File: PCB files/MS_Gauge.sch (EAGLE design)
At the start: 27 parts, among them IC1 B1836M, IC2 LPC11C24_QFP48, U1 MCP1700, U2 TSR1-2450, Y1 12MHz

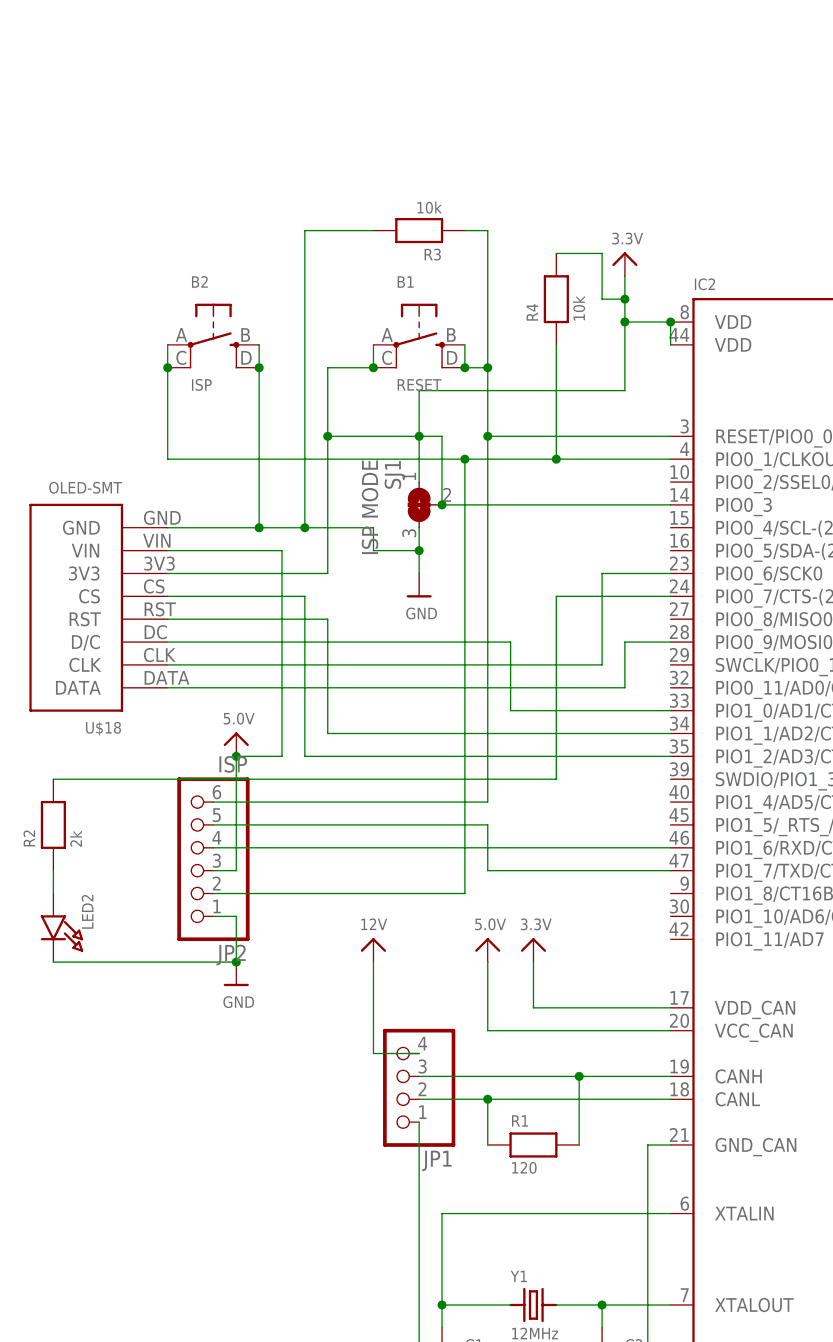
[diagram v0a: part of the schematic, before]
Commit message: Update Eagle files to Rev 4. Fixes wrong reset button wiring, adds termination resistor solder jumper.
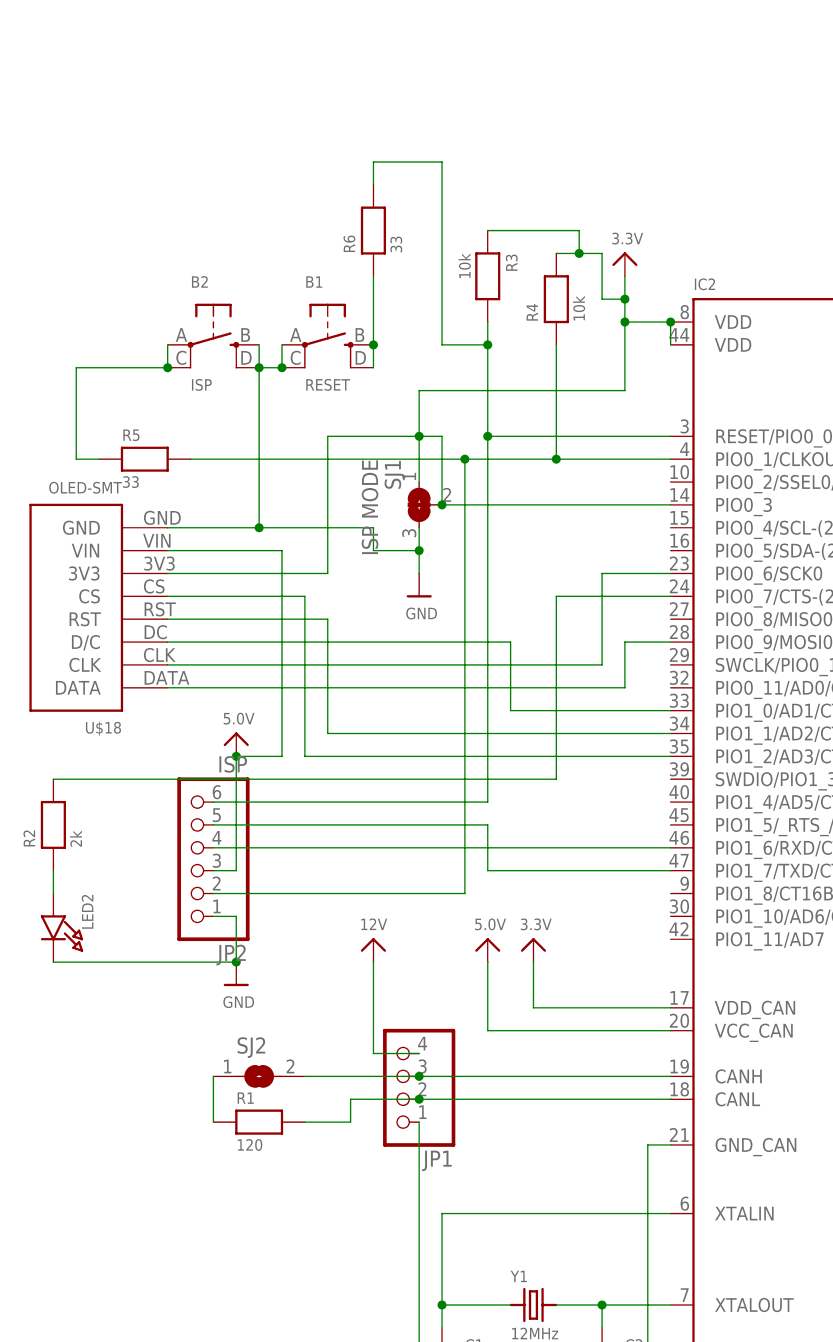
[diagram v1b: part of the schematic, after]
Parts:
- added R5, R6: 33, microbuilder:RESISTOR0603
- added SJ2: (no value), microbuilder:SOLDERJUMPER
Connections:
- new net N$17: IC2.CANH, JP1.3, SJ2.2
- new net N$6: IC2.PIO0_1/CLKOUT/CT32B0_MAT2, JP2.2, R4.1, R5.2
- new net N$8: B1.S, B1.S1, R6.1
- net 3.3V: now also R3.1; no longer B1.P, B1.P1
- net GND: now also B1.P, B1.P1; no longer R3.2
- net N$1: now also R1.1, SJ2.1; no longer IC2.CANH, JP1.3, R1.2
- net N$13: now also R3.2, R6.2; no longer B1.S, B1.S1, R3.1
- net N$2: now also R1.2; no longer R1.1
- net N$5: now also R5.1; no longer IC2.PIO0_1/CLKOUT/CT32B0_MAT2, JP2.2, R4.1
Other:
- moved on the sheet: B1, R1, R3

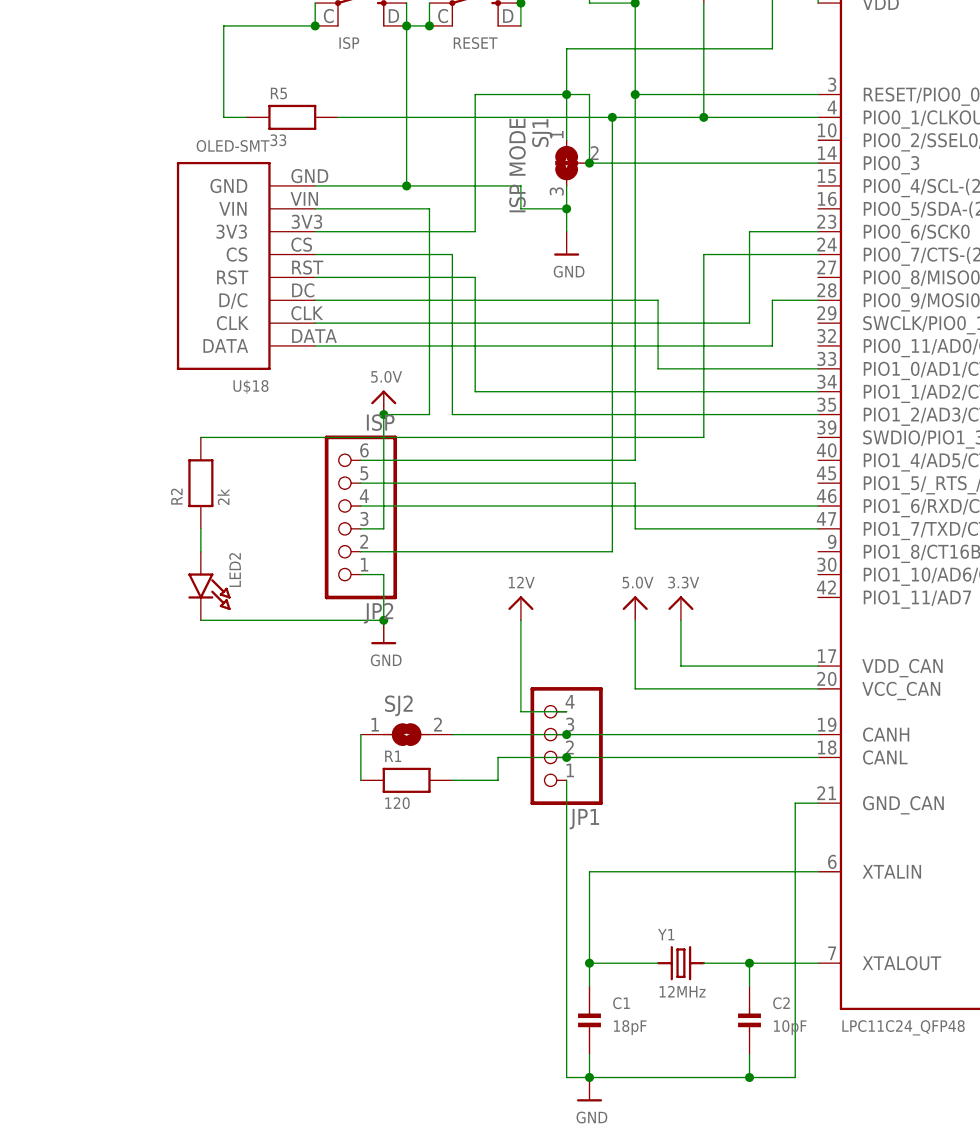
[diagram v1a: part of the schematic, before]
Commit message: Update Eagle files to Rev 5. Adds i2c eeprom.
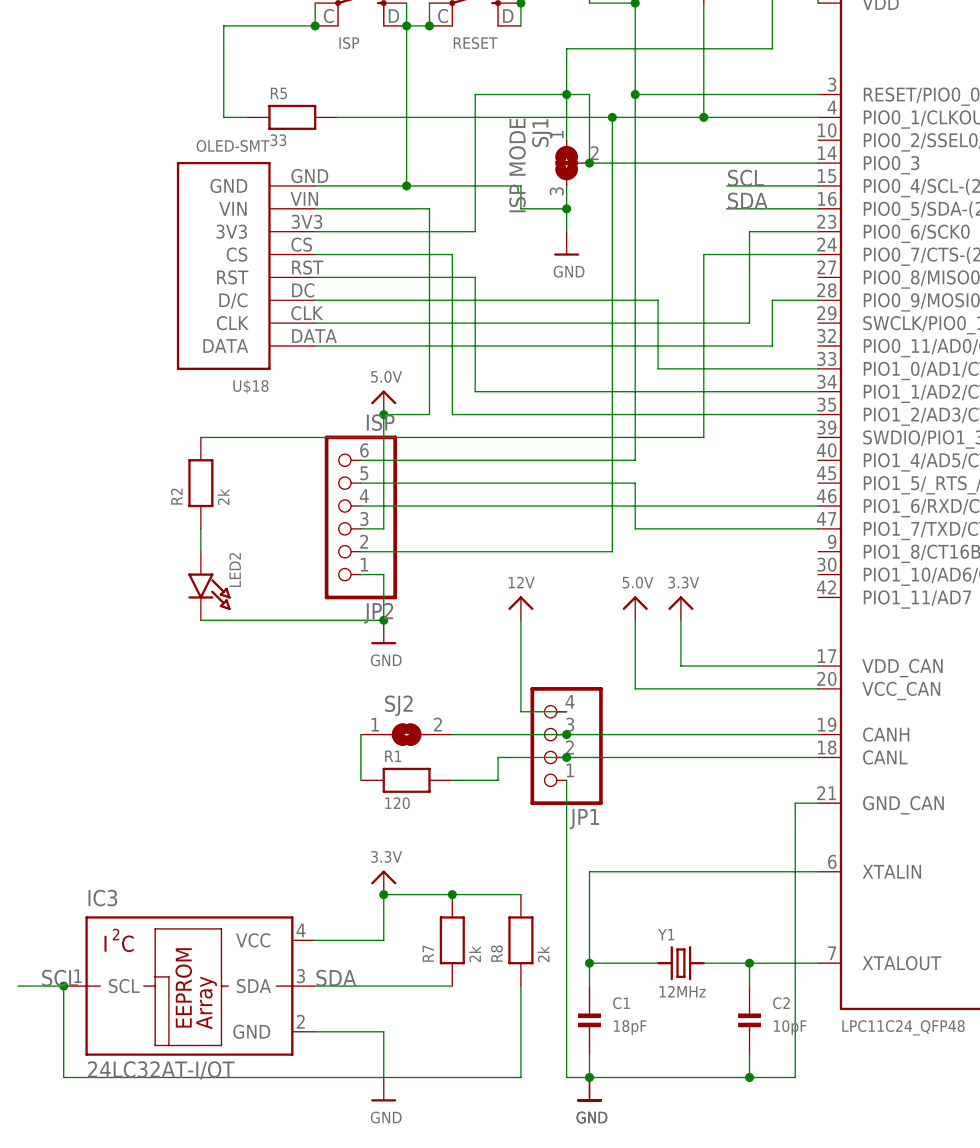
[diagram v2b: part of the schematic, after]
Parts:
- added IC3: 24LC32AT-I/OT, microchip:24LC32AT-I/OT
- added R7, R8: 2k, microbuilder:RESISTOR0603
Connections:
- new net SCL: IC2.PIO0_4/SCL-(20MA_SINK), IC3.SCL, R8.1
- new net SDA: IC2.PIO0_5/SDA-(20MA_SINK), IC3.SDA, R7.1
- net 3.3V: now also IC3.VCC, R7.2, R8.2
- net GND: now also IC3.GND
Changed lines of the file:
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@@
 <grid distance="0.1" unitdist="inch" unit="inch" style="lines" multiple="1" display="no" altdistance="0.01" altunitdist="inch" altunit="inch"/>
 <layers>
-<layer number="1" name="Top" color="4" fill="1" visible="no" active="no"/>
-<layer number="16" name="Bottom" color="1" fill="1" visible="no" active="no"/>
-<layer number="17" name="Pads" color="2" fill="1" visible="no" active="no"/>
-<layer number="18" name="Vias" color="2" fill="1" visible="no" active="no"/>
-<layer number="19" name="Unrouted" color="6" fill="1" visible="no" active="no"/>
-<layer number="20" name="Dimension" color="15" fill="1" visible="no" active="no"/>
-<layer number="21" name="tPlace" color="7" fill="1" visible="no" active="no"/>
-<layer number="22" name="bPlace" color="7" fill="1" visible="no" active="no"/>
-<layer number="23" name="tOrigins" color="15" fill="1" visible="no" active="no"/>
-<layer number="24" name="bOrigins" color="15" fill="1" visible="no" active="no"/>
-<layer number="25" name="tNames" color="7" fill="1" visible="no" active="no"/>
-<layer number="26" name="bNames" color="7" fill="1" visible="no" active="no"/>
-<layer number="27" name="tValues" color="7" fill="1" visible="no" active="no"/>
-<layer number="28" name="bValues" color="7" fill="1" visible="no" active="no"/>
+<layer number="1" name="Top" color="4" fill="1" visible="yes" active="no"/>
+<layer number="16" name="Bottom" color="1" fill="1" visible="yes" active="no"/>
+<layer number="17" name="Pads" color="2" fill="1" visible="yes" active="no"/>
+<layer number="18" name="Vias" color="2" fill="1" visible="yes" active="no"/>
+<layer number="19" name="Unrouted" color="6" fill="1" visible="yes" active="no"/>
+<layer number="20" name="Dimension" color="15" fill="1" visible="yes" active="no"/>
+<layer number="21" name="tPlace" color="7" fill="1" visible="yes" active="no"/>
+<layer number="22" name="bPlace" color="7" fill="1" visible="yes" active="no"/>
+<layer number="23" name="tOrigins" color="15" fill="1" visible="yes" active="no"/>
+<layer number="24" name="bOrigins" color="15" fill="1" visible="yes" active="no"/>
+<layer number="25" name="tNames" color="7" fill="1" visible="yes" active="no"/>
+<layer number="26" name="bNames" color="7" fill="1" visible="yes" active="no"/>
+<layer number="27" name="tValues" color="7" fill="1" visible="yes" active="no"/>
+<layer number="28" name="bValues" color="7" fill="1" visible="yes" active="no"/>
 <layer number="29" name="tStop" color="7" fill="3" visible="no" active="no"/>
 <layer number="30" name="bStop" color="7" fill="6" visible="no" active="no"/>
@@
 <layer number="35" name="tGlue" color="7" fill="4" visible="no" active="no"/>
 <layer number="36" name="bGlue" color="7" fill="5" visible="no" active="no"/>
-<layer number="37" name="tTest" color="7" fill="1" visible="no" active="no"/>
-<layer number="38" name="bTest" color="7" fill="1" visible="no" active="no"/>
+<layer number="37" name="tTest" color="7" fill="1" visible="yes" active="no"/>
+<layer number="38" name="bTest" color="7" fill="1" visible="yes" active="no"/>
 <layer number="39" name="tKeepout" color="4" fill="11" visible="no" active="no"/>
 <layer number="40" name="bKeepout" color="1" fill="11" visible="no" active="no"/>
@@
 <layer number="44" name="Drills" color="7" fill="1" visible="no" active="no"/>
 <layer number="45" name="Holes" color="7" fill="1" visible="no" active="no"/>
-<layer number="46" name="Milling" color="3" fill="1" visible="no" active="no"/>
-<layer number="47" name="Measures" color="7" fill="1" visible="no" active="no"/>
-<layer number="48" name="Document" color="7" fill="1" visible="no" active="no"/>
-<layer number="49" name="Reference" color="7" fill="1" visible="no" active="no"/>
-<layer number="50" name="dxf" color="7" fill="1" visible="no" active="no"/>
-<layer number="51" name="tDocu" color="7" fill="1" visible="no" active="no"/>
-<layer number="52" name="bDocu" color="7" fill="1" visible="no" active="no"/>
-<layer number="53" name="tGND_GNDA" color="7" fill="9" visible="no" active="no"/>
-<layer number="54" name="bGND_GNDA" color="1" fill="9" visible="no" active="no"/>
-<layer number="56" name="wert" color="7" fill="1" visible="no" active="no"/>
-<layer number="57" name="tCAD" color="7" fill="1" visible="no" active="no"/>
-<layer number="59" name="tCarbon" color="7" fill="1" visible="no" active="no"/>
-<layer number="60" name="bCarbon" color="7" fill="1" visible="no" active="no"/>
+<layer number="46" name="Milling" color="3" fill="1" visible="yes" active="no"/>
+<layer number="47" name="Measures" color="7" fill="1" visible="yes" active="no"/>
+<layer number="48" name="Document" color="7" fill="1" visible="yes" active="no"/>
+<layer number="49" name="Reference" color="7" fill="1" visible="yes" active="no"/>
+<layer number="50" name="dxf" color="7" fill="1" visible="yes" active="no"/>
+<layer number="51" name="tDocu" color="7" fill="1" visible="yes" active="no"/>
+<layer number="52" name="bDocu" color="7" fill="1" visible="yes" active="no"/>
+<layer number="53" name="tGND_GNDA" color="7" fill="9" visible="yes" active="no"/>
+<layer number="54" name="bGND_GNDA" color="1" fill="9" visible="yes" active="no"/>
+<layer number="56" name="wert" color="7" fill="1" visible="yes" active="no"/>
+<layer number="57" name="tCAD" color="7" fill="1" visible="yes" active="no"/>
+<layer number="59" name="tCarbon" color="7" fill="1" visible="yes" active="no"/>
+<layer number="60" name="bCarbon" color="7" fill="1" visible="yes" active="no"/>
 <layer number="90" name="Modules" color="5" fill="1" visible="yes" active="yes"/>
 <layer number="91" name="Nets" color="2" fill="1" visible="yes" active="yes"/>
@@
 <part name="R6" library="microbuilder" deviceset="RESISTOR" device="0603" value="33"/>
 <part name="SJ2" library="microbuilder" deviceset="SOLDERJUMPER" device=""/>
+<part name="U$21" library="microbuilder" deviceset="3.3V" device=""/>
+<part name="U$22" library="microbuilder" deviceset="GND" device=""/>
+<part name="U$23" library="microbuilder" deviceset="GND" device=""/>
+<part name="R7" library="microbuilder" deviceset="RESISTOR" device="0603" value="2k"/>
+<part name="R8" library="microbuilder" deviceset="RESISTOR" device="0603" value="2k"/>
+<part name="IC3" library="microchip" deviceset="24LC32AT-I/OT" device=""/>
 </parts>
 <sheets>
@@
 <instance part="R6" gate="G$1" x="-58.42" y="116.84" rot="R90"/>
 <instance part="SJ2" gate="1" x="-71.12" y="22.86"/>
+<instance part="U$21" gate="G$1" x="-73.66" y="7.62"/>
+<instance part="U$22" gate="G$1" x="-50.8" y="-17.78"/>
+<instance part="U$23" gate="G$1" x="-73.66" y="-17.78"/>
+<instance part="R7" gate="G$1" x="-66.04" y="0" rot="R90"/>
+<instance part="R8" gate="G$1" x="-58.42" y="0" rot="R90"/>
+<instance part="IC3" gate="G$1" x="-96.52" y="-5.08"/>
 </instances>
 <busses>
@@
 <wire x1="-27.94" y1="-15.24" x2="-33.02" y2="-15.24" width="0.1524" layer="91"/>
 <junction x="-33.02" y="-15.24"/>
+<pinref part="U$22" gate="G$1" pin="GND"/>
 </segment>
 <segment>
@@
 <wire x1="88.9" y1="2.54" x2="88.9" y2="0" width="0.1524" layer="91"/>
 <junction x="88.9" y="0"/>
+</segment>
+<segment>
+<wire x1="-81.28" y1="-10.16" x2="-73.66" y2="-10.16" width="0.1524" layer="91"/>
+<pinref part="U$23" gate="G$1" pin="GND"/>
+<wire x1="-73.66" y1="-15.24" x2="-73.66" y2="-10.16" width="0.1524" layer="91"/>
+<pinref part="IC3" gate="G$1" pin="GND"/>
 </segment>
 </net>
@@
 <wire x1="93.98" y1="15.24" x2="93.98" y2="17.78" width="0.1524" layer="91"/>
 </segment>
+<segment>
+<wire x1="-81.28" y1="0" x2="-73.66" y2="0" width="0.1524" layer="91"/>
+<pinref part="U$21" gate="G$1" pin="3.3V"/>
+<wire x1="-73.66" y1="0" x2="-73.66" y2="5.08" width="0.1524" layer="91"/>
+<pinref part="R8" gate="G$1" pin="2"/>
+<pinref part="R7" gate="G$1" pin="2"/>
+<wire x1="-58.42" y1="5.08" x2="-66.04" y2="5.08" width="0.1524" layer="91"/>
+<wire x1="-66.04" y1="5.08" x2="-73.66" y2="5.08" width="0.1524" layer="91"/>
+<junction x="-66.04" y="5.08"/>
+<junction x="-73.66" y="5.08"/>
+<pinref part="IC3" gate="G$1" pin="VCC"/>
+</segment>
 </net>
 <net name="N$18" class="0">
@@
 </segment>
 </net>
+<net name="SCL" class="0">
+<segment>
+<pinref part="IC2" gate="G$1" pin="PIO0_4/SCL-(20MA_SINK)"/>
+<wire x1="-25.4" y1="83.82" x2="-35.56" y2="83.82" width="0.1524" layer="91"/>
+<label x="-35.56" y="83.82" size="1.778" layer="95"/>
+</segment>
+<segment>
+<wire x1="-109.22" y1="-5.08" x2="-114.3" y2="-5.08" width="0.1524" layer="91"/>
+<label x="-111.76" y="-5.08" size="1.778" layer="95"/>
+<pinref part="R8" gate="G$1" pin="1"/>
+<wire x1="-58.42" y1="-5.08" x2="-58.42" y2="-15.24" width="0.1524" layer="91"/>
+<wire x1="-58.42" y1="-15.24" x2="-109.22" y2="-15.24" width="0.1524" layer="91"/>
+<wire x1="-109.22" y1="-15.24" x2="-109.22" y2="-5.08" width="0.1524" layer="91"/>
+<pinref part="IC3" gate="G$1" pin="SCL"/>
+<junction x="-109.22" y="-5.08"/>
+</segment>
+</net>
+<net name="SDA" class="0">
+<segment>
+<pinref part="IC2" gate="G$1" pin="PIO0_5/SDA-(20MA_SINK)"/>
+<wire x1="-25.4" y1="81.28" x2="-35.56" y2="81.28" width="0.1524" layer="91"/>
+<label x="-35.56" y="81.28" size="1.778" layer="95"/>
+</segment>
+<segment>
+<label x="-81.28" y="-5.08" size="1.778" layer="95"/>
+<pinref part="R7" gate="G$1" pin="1"/>
+<wire x1="-66.04" y1="-5.08" x2="-81.28" y2="-5.08" width="0.1524" layer="91"/>
+<pinref part="IC3" gate="G$1" pin="SDA"/>
+</segment>
+</net>
